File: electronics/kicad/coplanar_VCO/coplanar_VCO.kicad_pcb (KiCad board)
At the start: 2 copper layers, 82 parts, among them J1 CONN_01, J2 CONN_01, P1 CONN_1, P2 a, P3 OUTPUT, P4 a, P5 OUTPUT, P6 OUTPUT, P7 OUTPUT, P8 a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

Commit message: coplanarizing further
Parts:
- removed C1: 10uF, Capacitors:1206
- removed C13, C18: 10 nF, Capacitors:0402
- removed C16, C21, C32, C35: 100 nF, Capacitors:0603
- removed C17, C19, C27, C36: 1 nF, Capacitors:0402
- removed C20, C24, C25, C29, C3: 0.1 uF, Capacitors:0603
- removed C26: 10 pF, Capacitor_SMD:C_0402_1005Metric
- removed C28, C33, C34: 1 nF, Resistor_SMD:R_0402_1005Metric
- removed C7: 100 pF, Capacitors:0402
- removed D1: BAT15-04, Package_TO_SOT_SMD:SOT-23
- removed L2: 220 nH, Capacitors:0402
- removed L3: 440 nH, Resistor_SMD:R_0402_1005Metric
- removed P2: a, TestPoint:TestPoint_Pad_1.5x1.5mm
- removed P3: OUTPUT, Connector_PinHeader_2.54mm:PinHeader_1x01_P2.54mm_Vertical
- removed R11, R13: 100, Capacitors:0805
- removed R12: 50, Capacitors:0805
- removed R14, R17: 1k, Capacitors:0402
- removed R16, R9: 10k, Resistor_SMD:R_0402_1005Metric
- removed R18, R2, R7: 10k, Capacitors:0402
- removed TPOP1: Voutput, TestPoint:TestPoint_Pad_1.0x1.0mm
- removed U1, U4, U5, U8, U9: SY100EP, Package_SO:SOIC-8_3.9x4.9mm_P1.27mm
- removed U10: CE3520K3, 0xDBFB7:4-Micro-X
- removed U3: HMC363, Package_SO:SOIC-8-1EP_3.9x4.9mm_P1.27mm_EP2.35x2.35mm
- removed U6: SKY65013, Package_TO_SOT_SMD:SOT-89-3_Handsoldering
- added D4: BAT15-04, Package_TO_SOT_SMD:SOT-23, F.Cu at (21.0, 47.6)
- C10, C14, C15: value 0.1 uF -> 1 nF; footprint Capacitors:0603 -> Resistor_SMD:R_0402_1005Metric
- C11: value 1 nF -> 100 nF; footprint Capacitors:0402 -> Capacitors:0603
- C22: value 1 nF -> 10 nF
- C31, R15: footprint Capacitors:0402 -> Resistor_SMD:R_0402_1005Metric
- C5, C6, C8: value 10 nF -> 1 nF
- C9: value 0.1 uF -> 100 nF
- L1: value 440 nH -> 220 nH
- P1: value CONN_1 -> a
- P5, P6, P7: value OUTPUT -> a; footprint Connector_PinHeader_2.54mm:PinHeader_1x01_P2.54mm_Vertical -> TestPoint:TestPoint_Pad_1.5x1.5mm
- R3: value PAT1220 -> 10k; footprint 0xDBFB7:PAT1220 -> Resistor_SMD:R_0402_1005Metric
- R4, R8: value 100 -> 10k; footprint Capacitors:0805 -> Resistor_SMD:R_0402_1005Metric
- R5: value 50 -> 10k; footprint Capacitors:0805 -> Resistor_SMD:R_0402_1005Metric
- R6: value 1k -> 10k; footprint Capacitors:0402 -> Resistor_SMD:R_0402_1005Metric
- moved D3 61.4 mm to (21.0, 43.0)
- moved R6 57.9 mm to (31.1, 49.7)
- moved C12 57.6 mm to (28.2, 49.7)
- moved R4 55.7 mm to (31.1, 47.8)
- moved P8 54.1 mm to (33.4, 42.5)
- moved TPSO1 51.7 mm to (31.6, 19.1)
- moved P5 48.9 mm to (25.0, 45.0)
- moved R5 40.9 mm to (34.7, 45.3)
- moved C11 39.3 mm to (29.6, 42.0)
- moved C15 38.8 mm to (43.8, 26.6)
- moved C9 35.7 mm to (25.3, 42.0)
- moved R8 31.5 mm to (34.0, 47.3)
- moved C14 30.3 mm to (40.1, 22.3)
- moved P6 27.9 mm to (28.5, 45.0)
- moved P7 27.8 mm to (25.0, 48.5)
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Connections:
- C10 pad 1: 3.3V -> Net-(C10-Pad1)
- C11 pad 1: GND -> Net-(C11-Pad1)
- C11 pad 2: Net-(C11-Pad2) -> GND
- C12 pad 1: GND -> Net-(C12-Pad1)
- C12 pad 2: 5V -> GND
- C14 pad 1: 5V -> Net-(C14-Pad1)
- C14 pad 2: GND -> Net-(C14-Pad2)
- C15 pad 1: 3.3V -> Net-(C15-Pad1)
- C15 pad 2: GND -> Net-(C14-Pad1)
- D2 pad 3: Net-(D2-Pad3) -> Net-(C14-Pad1)
- D3 pad 1: GND -> Net-(D3-Pad1)
- D3 pad 2: Net-(C36-Pad1) -> Net-(C10-Pad1)
- D3 pad 3: Net-(D3-Pad3) -> Net-(C15-Pad1)
- L1 pad 2: Net-(C26-Pad1) -> Net-(C14-Pad2)
- P1 pad 1: Net-(C7-Pad2) -> Net-(C31-Pad1)
- P5 pad 1: GND -> Net-(C10-Pad1)
- P6 pad 1: 3.3V -> Net-(C9-Pad1)
- P7 pad 1: Net-(P7-Pad1) -> Net-(C12-Pad1)
- P8 pad 1: Net-(C35-Pad1) -> Net-(C11-Pad1)
- R10 pad 1: Net-(C18-Pad1) -> Net-(R10-Pad1)
- R3 pad 1: Net-(C7-Pad1) -> Net-(C30-Pad1)
- R3 pad 2: Net-(R3-Pad2) -> Net-(C31-Pad1)
- R4 pad 1: Net-(R4-Pad1) -> Net-(C9-Pad1)
- R4 pad 2: GND -> Net-(C10-Pad1)
- R5 pad 1: GND -> Net-(C10-Pad1)
- R5 pad 2: Net-(R5-Pad2) -> GND
- R6 pad 1: Net-(C16-Pad1) -> Net-(C11-Pad1)
- R6 pad 2: Net-(C17-Pad1) -> Net-(C12-Pad1)
- R8 pad 1: Net-(R8-Pad1) -> Net-(C12-Pad1)
- U2 pad 1: (no net) -> GND
- U2 pad 15: Net-(C13-Pad2) -> Net-(R10-Pad1)
- U2 pad 2: (no net) -> GND
- U2 pad 23: (no net) -> GND
- U2 pad 24: (no net) -> GND
- U2 pad 3: (no net) -> GND
- U7 pad 2: Net-(C26-Pad1) -> Net-(C14-Pad2)
- U7 pad 4: Net-(C18-Pad1) -> Net-(R10-Pad1)
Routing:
- net Net-(C14-Pad2): track 0.00 -> 8.40 mm
- net 5V: track 0.00 -> 3.96 mm
- net Net-(R10-Pad1): track 0.00 -> 2.71 mm
- net Net-(C4-Pad1): track 0.00 -> 2.38 mm

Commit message: Coplanar
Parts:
- moved C31 45.6 mm to (36.6, 23.7), turned to 180 degrees
- moved R15 38.4 mm to (36.6, 24.5), turned to 180 degrees
- moved C30 34.4 mm to (35.4, 28.7), turned to 180 degrees
- moved P7 34.2 mm to (36.6, 16.4)
- moved R6 34.1 mm to (39.2, 16.6), turned to 270 degrees
- moved C12 34.1 mm to (40.7, 18.0), turned to 90 degrees
- moved D4 33.5 mm to (39.1, 19.5), turned to 150 degrees
- moved P4 32.8 mm to (37.6, 28.7)
- moved R8 30.2 mm to (41.6, 18.0), turned to 90 degrees
- moved D2 29.4 mm to (36.6, 21.8), turned to 90 degrees
- moved C11 29.4 mm to (41.4, 15.1)
- moved D3 29.0 mm to (40.8, 21.8), turned to 90 degrees
- moved P8 28.1 mm to (39.2, 15.1)
- moved R3 26.9 mm to (37.6, 27.1), turned to 90 degrees
- moved P5 25.4 mm to (41.2, 25.6)
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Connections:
- U2 pad 10: (no net) -> GND
- U2 pad 11: (no net) -> GND
- U2 pad 13: (no net) -> GND
- U2 pad 16: (no net) -> GND
- U2 pad 17: (no net) -> GND
- U2 pad 18: (no net) -> GND
- U2 pad 19: (no net) -> GND
- U2 pad 20: (no net) -> GND
- U2 pad 21: (no net) -> GND
- U2 pad 22: (no net) -> GND
- U2 pad 5: (no net) -> GND
- U2 pad 6: (no net) -> GND
- U2 pad 7: (no net) -> GND
- U2 pad 8: (no net) -> GND
- U2 pad 9: (no net) -> GND
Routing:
- net Net-(C15-Pad1): track 0.00 -> 10.3 mm
- net Net-(C12-Pad1): track 0.00 -> 7.15 mm
- net Net-(C31-Pad1): track 0.00 -> 4.23 mm
- net Net-(C10-Pad1): track 0.00 -> 4.00 mm
- net Net-(C14-Pad2): track 8.40 -> 4.80 mm
- net Net-(C30-Pad1): track 0.00 -> 2.38 mm
- net Net-(C9-Pad1): track 0.00 -> 2.27 mm
- net Net-(C14-Pad1): track 0.00 -> 1.24 mm
- added copper zone on F.Cu, net GND

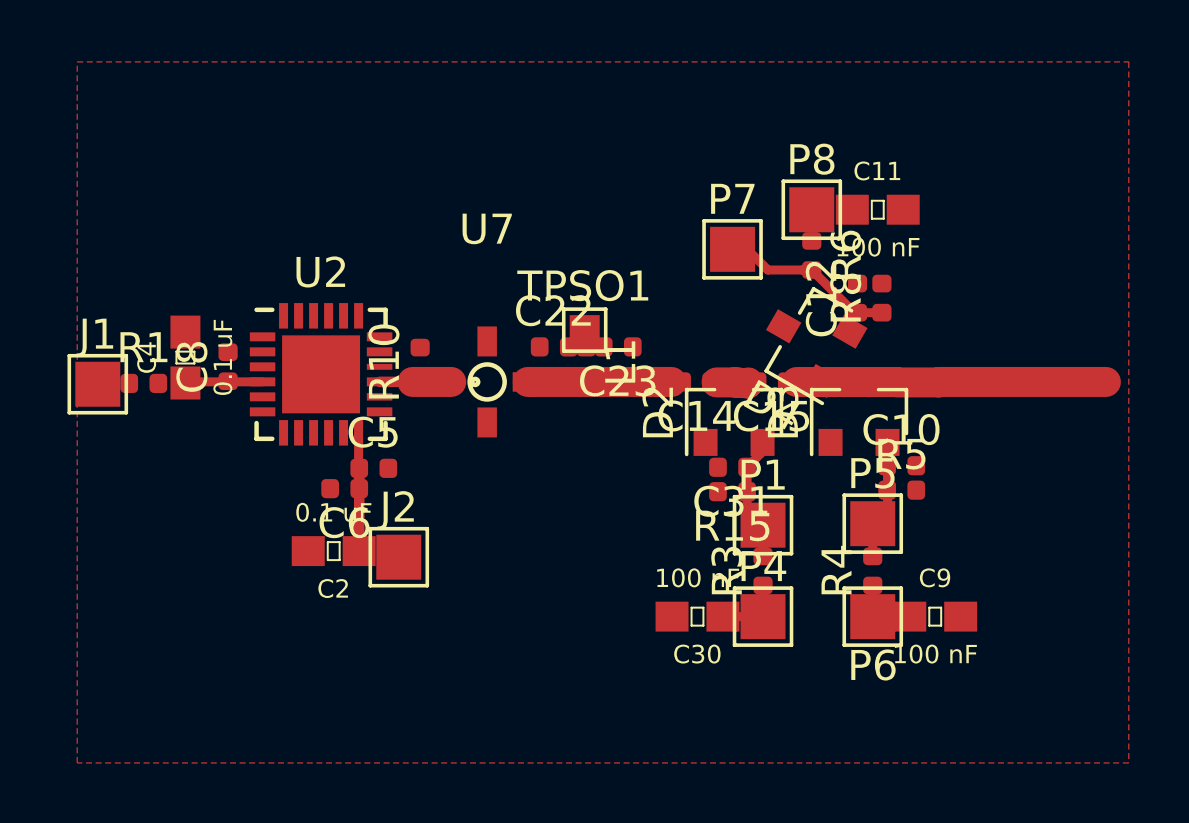
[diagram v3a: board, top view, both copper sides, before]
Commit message: integrated amp
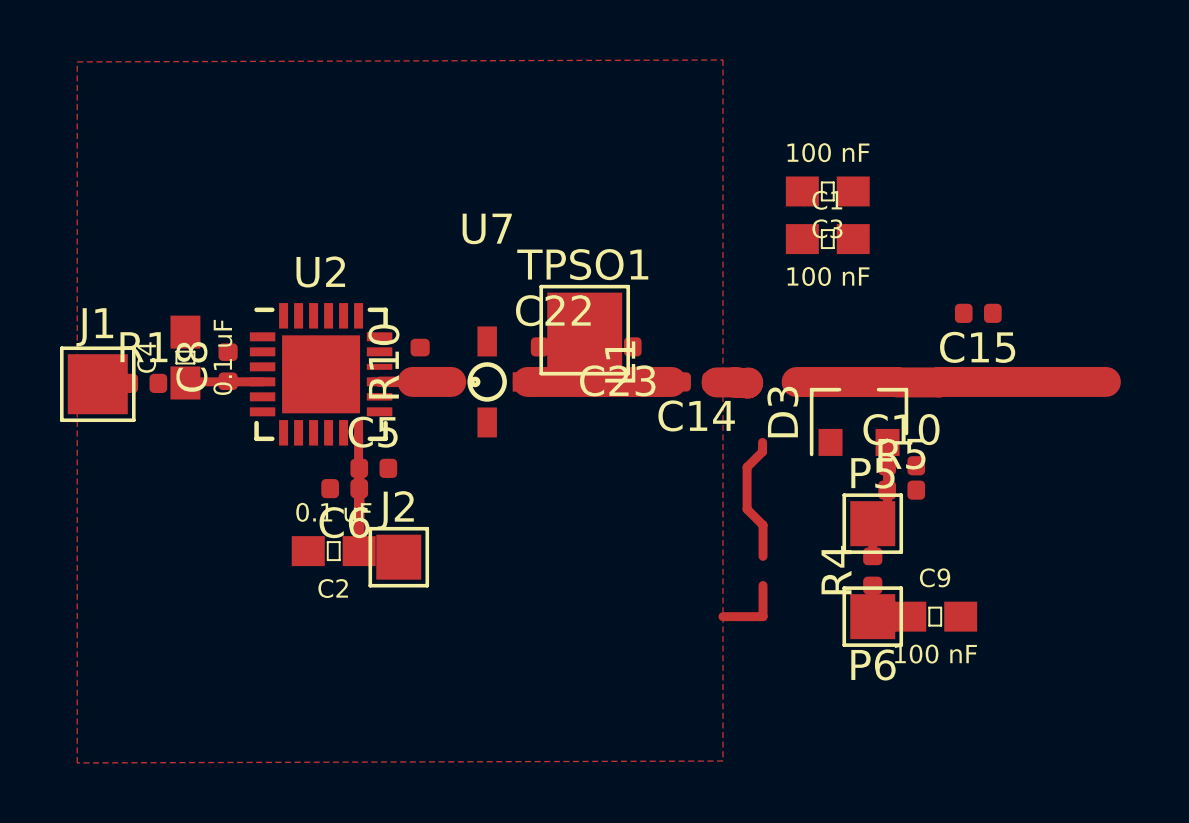
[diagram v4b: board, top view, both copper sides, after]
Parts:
- removed C11, C30: 100 nF, Capacitors:0603
- removed C12, C31: 1 nF, Resistor_SMD:R_0402_1005Metric
- removed D2, D4: BAT15-04, Package_TO_SOT_SMD:SOT-23
- removed P1, P4, P7, P8: a, TestPoint:TestPoint_Pad_1.5x1.5mm
- removed R15, R3, R6, R8: 10k, Resistor_SMD:R_0402_1005Metric
- added C1: 100 nF, Capacitors:0603, F.Cu at (39.8, 16.1)
- added C3: 100 nF, Capacitors:0603, F.Cu at (39.8, 14.5)
- J1: footprint TestPoint:TestPoint_Pad_1.5x1.5mm -> TestPoint:TestPoint_Pad_2.0x2.0mm
- TPSO1: footprint TestPoint:TestPoint_Pad_1.0x1.0mm -> TestPoint:TestPoint_Pad_2.5x2.5mm
- moved C15 7.24 mm to (44.8, 18.5)
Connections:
- D3 pad 3: Net-(C15-Pad1) -> Net-(C14-Pad1)
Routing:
- net Net-(C15-Pad1): track 10.3 -> 0.00 mm
- net Net-(C14-Pad1): track 1.24 -> 11.5 mm
- net Net-(C12-Pad1): track 7.15 -> 0.00 mm
